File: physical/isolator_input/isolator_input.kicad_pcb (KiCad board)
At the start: 2 copper layers, 27.3 x 27.3 mm, 20 parts, among them J1 Output, J2 Input, Q1 PN2222A, Q2 PN2222A, U1 H11L1, U2 H11L1

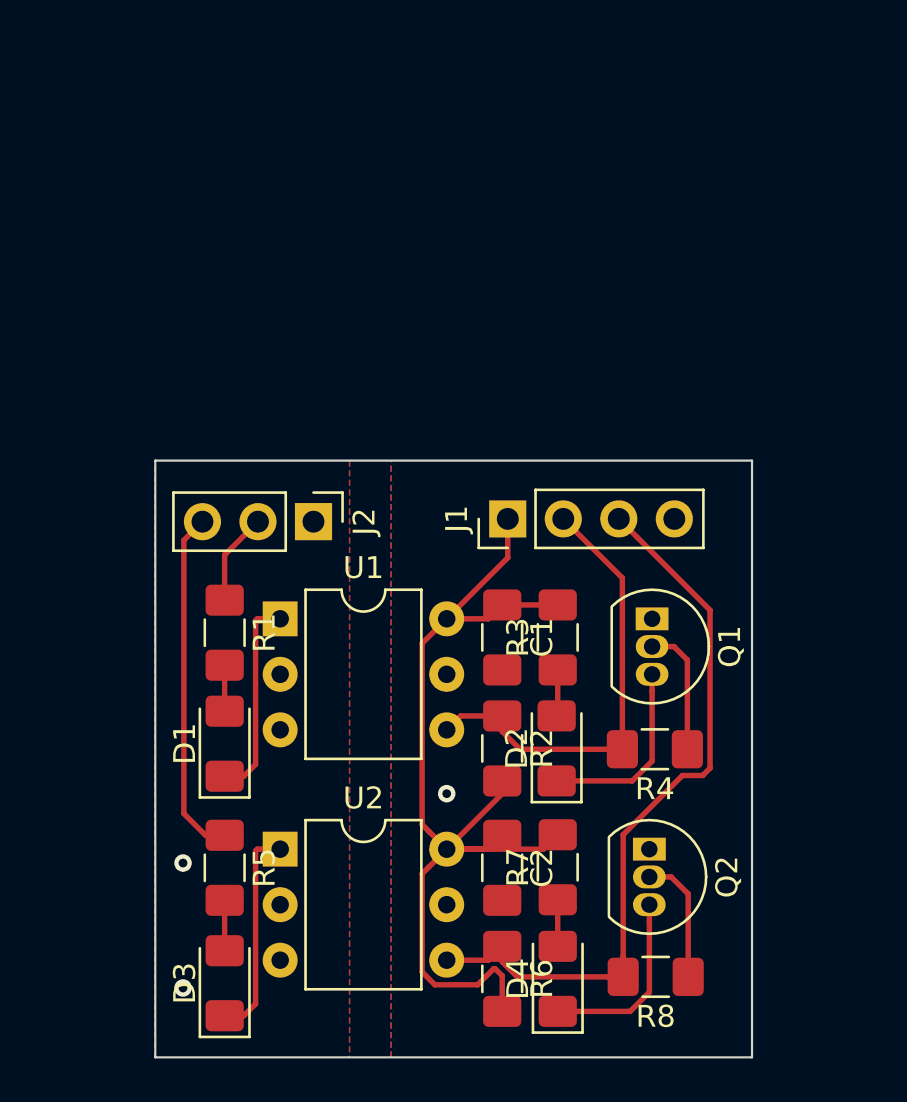
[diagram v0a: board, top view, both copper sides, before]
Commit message: opto-isolator board op-amp indicator
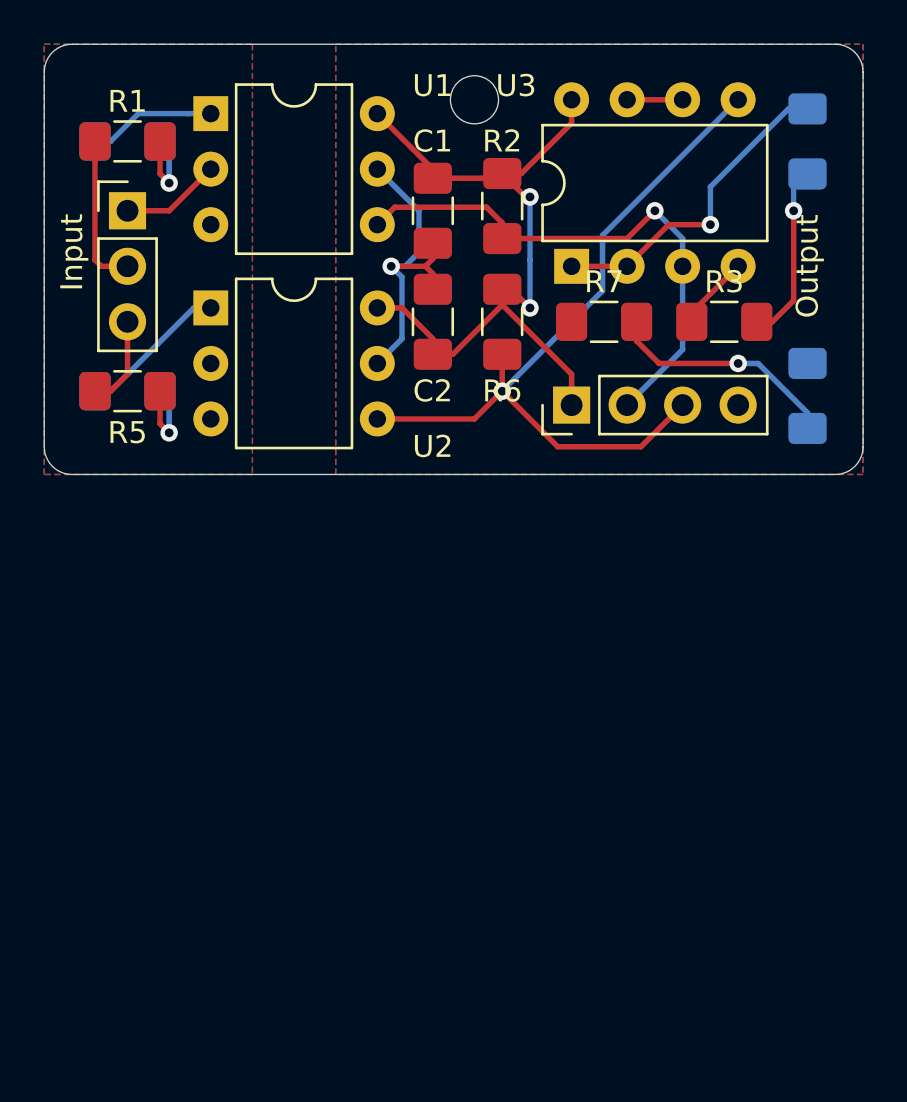
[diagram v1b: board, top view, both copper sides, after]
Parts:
- removed Q1, Q2: PN2222A, Package_TO_SOT_THT:TO-92_Inline
- removed R4, R8: 1k, Resistor_SMD:R_1206_3216Metric_Pad1.42x1.75mm_HandSolder
- added REF**: MountingHole_2.2mm_M2_DIN965, MountingHole:MountingHole_2.2mm_M2_DIN965, F.Cu at (44.5, 40.6)
- added U3: MCP6002-xSN, Package_DIP:DIP-8_W7.62mm, F.Cu at (48.9, 48.3)
- D1, D2, D3, D4: moved to B.Cu
- Input: renamed from J2; value Input -> Conn_01x03_Male
- Output: renamed from J1; value Output -> Conn_01x04_Male
- moved R6 30.1 mm to (45.7, 50.8), turned to 90 degrees
- moved D2 30.1 mm to (59.7, 42.5)
- moved D4 29.0 mm to (59.7, 54.2)
- moved D1 27.9 mm to (28.6, 42.5), turned to 0 degrees
- moved D3 27.4 mm to (28.6, 54.0), turned to 0 degrees
- moved C2 25.2 mm to (42.5, 50.8), turned to 90 degrees
- moved R7 25.0 mm to (50.4, 50.8), turned to 0 degrees
- moved U2 25.0 mm to (32.4, 50.2)
- moved R2 24.8 mm to (45.7, 45.5), turned to 90 degrees
- moved U1 23.3 mm to (32.4, 41.3)
- moved R1 22.9 mm to (28.6, 42.5), turned to 0 degrees
- moved R5 22.3 mm to (28.6, 54.0), turned to 0 degrees
- moved C1 19.8 mm to (42.5, 45.7)
- moved Input 16.6 mm to (28.6, 45.7), turned to 0 degrees
- moved R3 16.3 mm to (55.9, 50.8), turned to 0 degrees
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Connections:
- R3 pad 1: Net-(D2-Pad2) -> GNDA
- R3 pad 2: +3V3 -> Net-(D2-Pad1)
- R7 pad 1: Net-(D4-Pad2) -> GNDA
- R7 pad 2: +3V3 -> Net-(D4-Pad1)
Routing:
- net GNDA: track 0.00 -> 18.6 mm
- net Net-(D2-Pad2): track 2.12 -> 14.8 mm, vias 0 -> 1
- net In02: track 16.0 -> 4.21 mm
- net +3V3: track 46.9 -> 35.5 mm, vias 0 -> 2
- net Net-(Q1-Pad2): track 5.95 -> 0.00 mm
- net Net-(Q2-Pad2): track 5.89 -> 0.00 mm
- net GND: track 0.00 -> 4.60 mm, vias 2 -> 0
- net Out01: track 21.0 -> 25.0 mm, vias 0 -> 1
- net Net-(D1-Pad1): track 9.38 -> 5.82 mm
- net Net-(D3-Pad1): track 9.80 -> 6.88 mm
- net In01: track 4.22 -> 7.04 mm
- net Net-(D4-Pad1): track 8.56 -> 10.8 mm, vias 0 -> 1
- net Net-(D1-Pad2): track 2.11 -> 4.16 mm, vias 0 -> 1
- net Net-(D3-Pad2): track 2.31 -> 4.16 mm, vias 0 -> 1
- net Out02: track 35.2 -> 35.8 mm, vias 0 -> 1
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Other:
- board size 27.3 x 27.3 mm -> 37.5 x 19.7 mm
- board text added: "0"
- board text added: "1"
- board text added: "2ch optical isolation"
- board text added: "BATTAGLIA LAB 2019 Designed by R.E."
- board text added: "GND"
- board text added: "Vin"
- board text added: "v0.2"

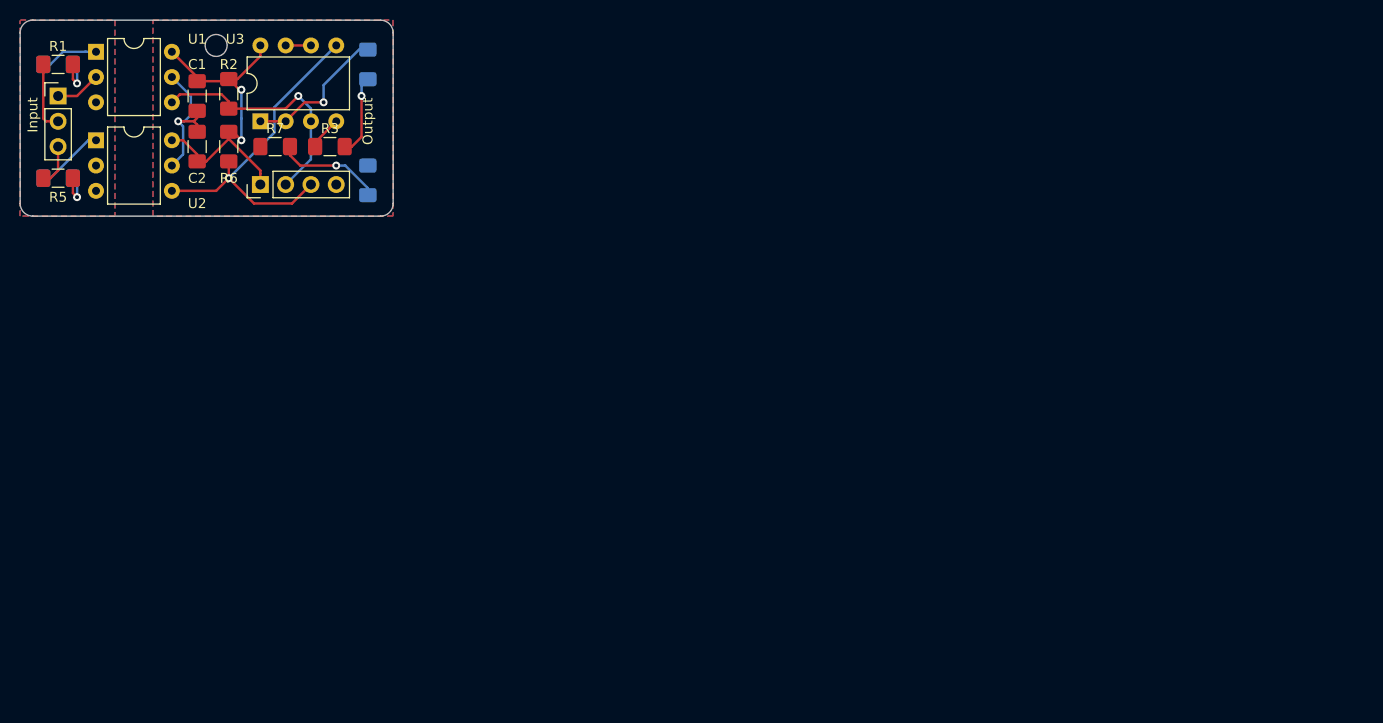
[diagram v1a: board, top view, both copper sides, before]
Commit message: reverse polarity LED indicator
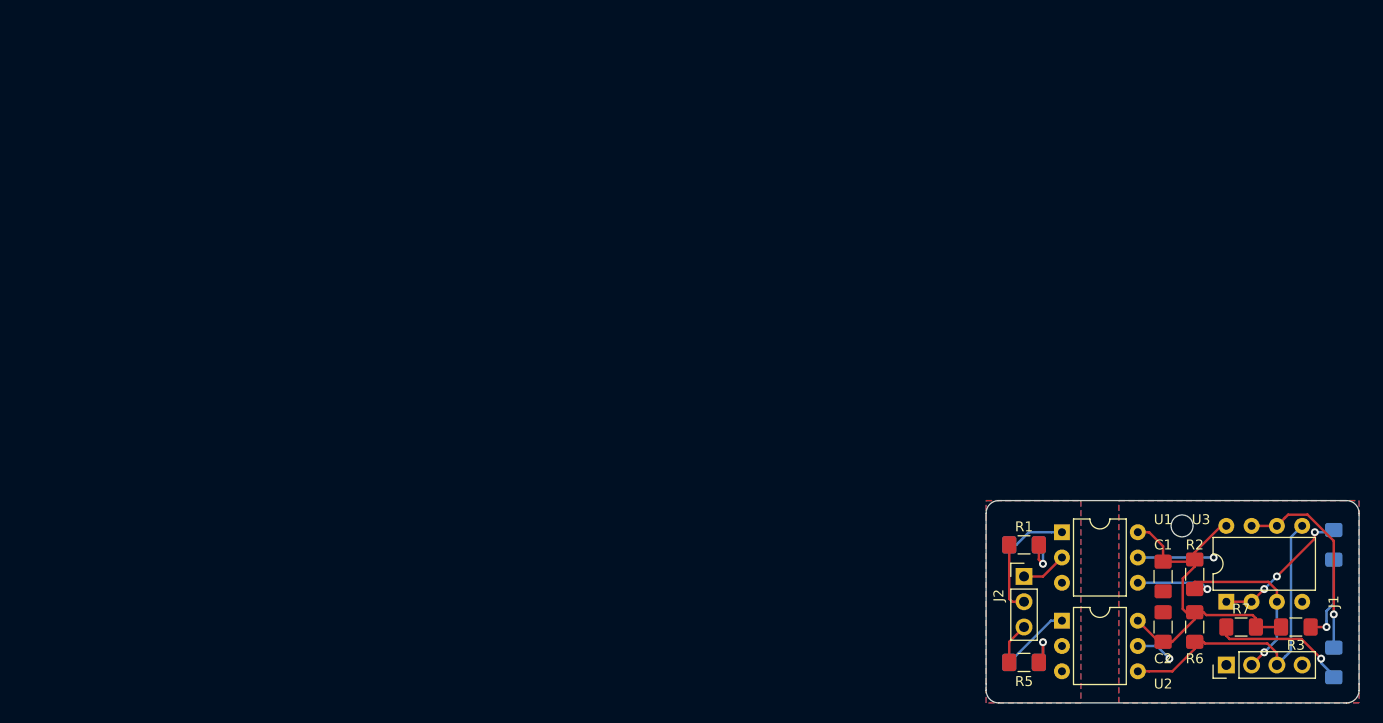
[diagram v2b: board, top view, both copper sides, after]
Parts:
- added G***: LOGO, mila:mila, B.Cu at (141.7, 96.5)
- moved D3 108.5 mm to (125.6, 102.6)
- moved R5 108.5 mm to (125.6, 102.6)
- moved D4 108.4 mm to (156.7, 102.6), turned to 270 degrees
- moved R7 108.4 mm to (147.4, 99.1)
- moved U1 108.4 mm to (129.4, 89.5)
- moved U2 108.4 mm to (129.4, 98.4)
- moved C1 108.4 mm to (139.6, 94.0)
- moved C2 108.4 mm to (139.6, 99.1)
- moved REF** 108.4 mm to (141.5, 88.9)
- moved D1 108.4 mm to (125.6, 90.8)
- moved D2 108.4 mm to (156.7, 90.8), turned to 270 degrees
- moved J1 108.4 mm to (145.9, 102.9)
- moved J2 108.4 mm to (125.6, 94.0)
- moved R1 108.4 mm to (125.6, 90.8)
- moved R2 108.4 mm to (142.7, 93.8)
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- renumbered Output to J1, Input to J2
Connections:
- C1 pad 1: +3V3 -> VDD
- C2 pad 1: +3V3 -> VDD
- J1 pad 1: +3V3 -> (no net)
- R2 pad 2: +3V3 -> VDD
- R3 pad 1: GNDA -> Net-(D2-Pad2)
- R3 pad 2: Net-(D2-Pad1) -> VDD
- R6 pad 2: +3V3 -> VDD
- R7 pad 1: GNDA -> Net-(D4-Pad2)
- R7 pad 2: Net-(D4-Pad1) -> VDD
- U1 pad 6: +3V3 -> VDD
- U2 pad 6: +3V3 -> VDD
- U3 pad 1: Net-(D2-Pad2) -> Net-(D2-Pad1)
- U3 pad 2: Net-(D2-Pad2) -> Net-(D2-Pad1)
- U3 pad 6: Net-(D4-Pad2) -> Net-(D4-Pad1)
- U3 pad 7: Net-(D4-Pad2) -> Net-(D4-Pad1)
- U3 pad 8: +3V3 -> VDD
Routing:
- net VDD: track 0.00 -> 37.8 mm
- net +3V3: track 35.5 -> 0.00 mm, vias 2 -> 0
- net Net-(D4-Pad2): track 2.54 -> 13.6 mm, vias 0 -> 1
- net Net-(D4-Pad1): track 10.8 -> 20.4 mm
- net GNDA: track 18.6 -> 11.3 mm, vias 1 -> 2
- net Net-(D2-Pad1): track 8.15 -> 14.2 mm, vias 1 -> 3
- net Net-(D2-Pad2): track 14.8 -> 9.38 mm
- net Out02: track 35.8 -> 32.3 mm, vias 1 -> 0
- net Out01: track 25.0 -> 27.0 mm, vias 1 -> 2
- net Net-(D3-Pad1): track 6.88 -> 7.81 mm
- net Net-(D3-Pad2): track 4.16 -> 5.00 mm
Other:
- board size 37.5 x 19.7 mm -> 37.5 x 20.3 mm
- board text added: "VDD"
- board text added: "v0.3"
- board text removed: "Vin"
- board text removed: "v0.2"

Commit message: Housekeeping
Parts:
- added REF**: MountingHole_2.2mm_M2_DIN965, MountingHole:MountingHole_2.2mm_M2_DIN965, F.Cu at (140.7, 104.3)
- moved REF** 0.77 mm to (140.7, 88.8)
- moved D1 0.67 mm to (124.9, 90.8)
- moved D3 0.67 mm to (124.9, 102.6)
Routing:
- net Out02: track 32.3 -> 16.9 mm
- net Net-(D3-Pad2): track 5.00 -> 3.61 mm
- net GNDA: track 11.3 -> 12.1 mm, vias 2 -> 1
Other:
- board size 37.5 x 20.3 mm -> 37.8 x 20.3 mm
